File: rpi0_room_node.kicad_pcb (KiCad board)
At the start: 2 copper layers, 65 x 30 mm, 41 parts, among them J1 Raspberry Pi, J2 Conn_01x03, J3 Conn_01x03, J4 Conn_01x03, Q1 PDTC123Y, U1 AP2210K-3.3, U2 TSOP382xx, U3 RFM69HCW

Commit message: Convert to KiCad 6 format
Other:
- net class ANT removed
- net class Default removed

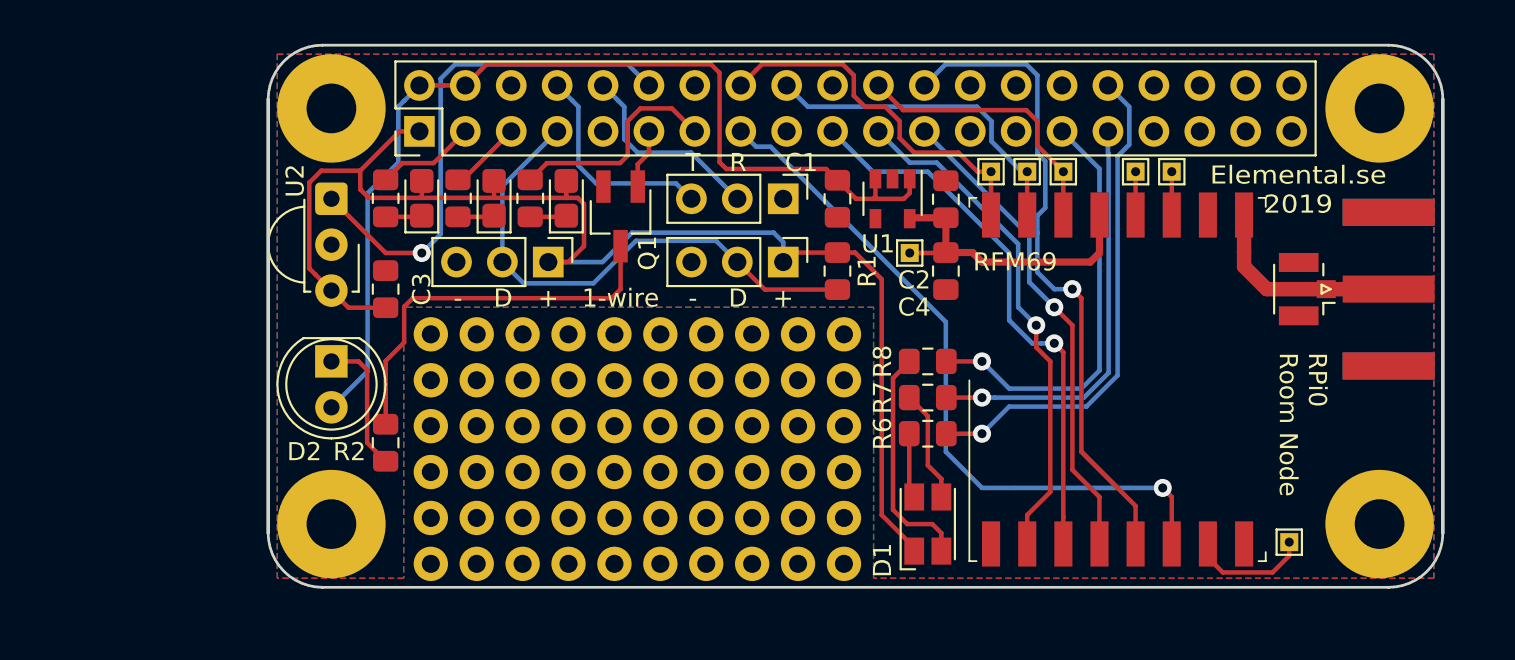
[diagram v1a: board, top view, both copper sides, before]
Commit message: Add ADS1015 ADC
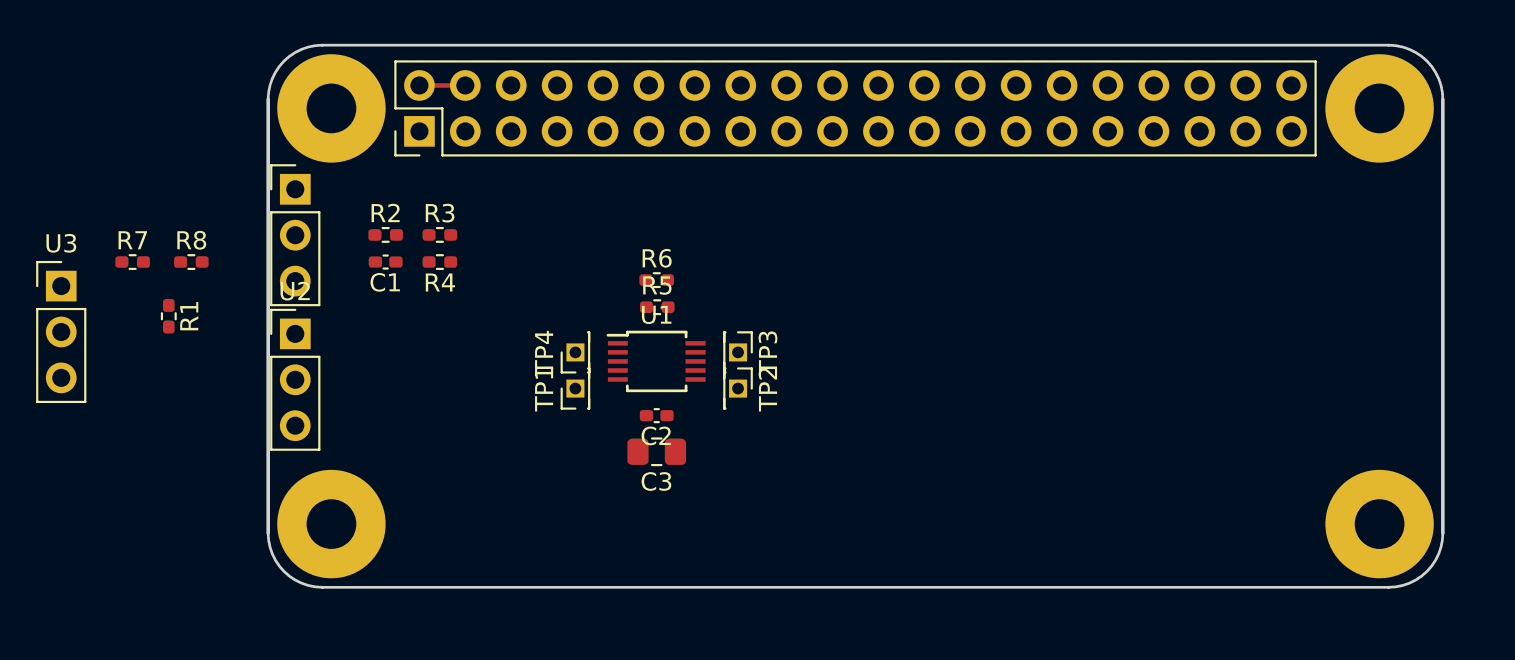
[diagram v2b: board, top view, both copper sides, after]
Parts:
- removed AE1: SMA, Connector_Coaxial:SMA_Amphenol_132289_EdgeMount
- removed AE2: U.FL, Connector_Coaxial:U.FL_Hirose_U.FL-R-SMT-1_Vertical
- removed C4: C, Capacitor_SMD:C_0805_2012Metric_Pad1.15x1.40mm_HandSolder
- removed D1: ASMB-MTB0-0A3A2, LED_SMD:LED_Avago_PLCC4_3.2x2.8mm_CW
- removed D2: CQY99, LED_THT:LED_D5.0mm_IRGrey
- removed D3, D4, D5: LED, LED_SMD:LED_0805_2012Metric_Castellated
- removed G***: LOGO, elemental:elemental-4mm-mask
- removed G***: LOGO, elemental:elemental-25.4mm
- removed J2, J4: Conn_01x03, Connector_PinHeader_2.54mm:PinHeader_1x03_P2.54mm_Vertical
- removed Q1: PDTC123Y, Package_TO_SOT_SMD:SC-59_Handsoldering
- removed REF**: protoarea, protoarea:protoarea
- removed TP5, TP6, TP7: TestPoint, TestPoint:TestPoint_THTPad_1.0x1.0mm_Drill0.5mm
- C1, C2: value C -> 100n; footprint Capacitor_SMD:C_0805_2012Metric_Pad1.15x1.40mm_HandSolder -> Capacitor_SMD:C_0402_1005Metric_Pad0.74x0.62mm_HandSolder
- C3: footprint Capacitor_SMD:C_0805_2012Metric_Pad1.15x1.40mm_HandSolder -> Capacitor_SMD:C_0805_2012Metric_Pad1.18x1.45mm_HandSolder
- R1, R2, R3, R4, R5, R6: footprint Resistor_SMD:R_0805_2012Metric_Pad1.15x1.40mm_HandSolder -> Resistor_SMD:R_0402_1005Metric_Pad0.72x0.64mm_HandSolder
- R7, R8: value R -> 10; footprint Resistor_SMD:R_0805_2012Metric_Pad1.15x1.40mm_HandSolder -> Resistor_SMD:R_0402_1005Metric_Pad0.72x0.64mm_HandSolder
- TP1, TP2, TP3, TP4: footprint TestPoint:TestPoint_THTPad_1.0x1.0mm_Drill0.5mm -> Connector_PinHeader_1.27mm:PinHeader_1x01_P1.27mm_Vertical
- U1: value AP2210K-3.3 -> ADS1015IDGS; footprint Package_TO_SOT_SMD:SOT-23-5 -> Package_SO:TSSOP-10_3x3mm_P0.5mm
- U2: value TSOP382xx -> DS18B20; footprint OptoDevice:Vishay_MINICAST-3Pin -> Connector_PinHeader_2.54mm:PinHeader_1x03_P2.54mm_Vertical
- U3: value RFM69HCW -> DS18B20; footprint RF_Module:HOPERF_RFM69HW -> Connector_PinHeader_2.54mm:PinHeader_1x03_P2.54mm_Vertical
- moved U3 58.7 mm to (85.0, 109.8), turned to 0 degrees
- moved R7 44.6 mm to (89.0, 108.5), turned to 0 degrees
- moved R8 41.1 mm to (92.2, 108.5), turned to 0 degrees
- moved TP1 40.4 mm to (113.5, 115.5), turned to 90 degrees
- moved R1 37.1 mm to (91.0, 111.5)
- moved J3 27.0 mm to (98.0, 104.5), turned to 0 degrees
- moved TP3 26.0 mm to (122.5, 113.5), turned to -90 degrees
- moved C1 25.2 mm to (103.0, 108.5), turned to 180 degrees
- moved TP4 25.1 mm to (113.5, 113.5), turned to 90 degrees
- moved TP2 25.1 mm to (122.5, 115.5), turned to -90 degrees
- moved C2 20.0 mm to (118.0, 117.0), turned to 180 degrees
- moved C3 17.5 mm to (118.0, 119.0), turned to 180 degrees
- moved R6 17.2 mm to (118.0, 109.5), turned to 0 degrees
- moved U1 15.9 mm to (118.0, 114.0), turned to 0 degrees
- moved R2 11.5 mm to (103.0, 107.0), turned to 0 degrees
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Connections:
- C1 pad 1: +5V -> /AIN0
- C2 pad 1: VDDA -> +3.3V
- C3 pad 1: +3V3 -> +3.3V
- J1 pad 1: +3V3 -> +3.3V
- J1 pad 10: /RXD -> unconnected-(J1-Pad10)
- J1 pad 11: /IRTX -> unconnected-(J1-Pad11)
- J1 pad 12: /IRRX -> unconnected-(J1-Pad12)
- J1 pad 13: /LED3 -> unconnected-(J1-Pad13)
- J1 pad 14: GND -> unconnected-(J1-Pad14)
- J1 pad 15: /RFM_RST -> unconnected-(J1-Pad15)
- J1 pad 16: /RFM_DIO2 -> unconnected-(J1-Pad16)
- J1 pad 17: Net-(J1-Pad17) -> unconnected-(J1-Pad17)
- J1 pad 18: /RFM_DIO1 -> unconnected-(J1-Pad18)
- J1 pad 19: /MOSI -> unconnected-(J1-Pad19)
- J1 pad 20: GND -> unconnected-(J1-Pad20)
- J1 pad 21: /MISO -> unconnected-(J1-Pad21)
- J1 pad 22: /RFM_DIO0 -> unconnected-(J1-Pad22)
- J1 pad 23: /SCLK -> unconnected-(J1-Pad23)
- J1 pad 24: /CE0 -> unconnected-(J1-Pad24)
- J1 pad 25: GND -> unconnected-(J1-Pad25)
- J1 pad 26: Net-(J1-Pad26) -> unconnected-(J1-Pad26)
- J1 pad 27: Net-(J1-Pad27) -> unconnected-(J1-Pad27)
- J1 pad 28: Net-(J1-Pad28) -> unconnected-(J1-Pad28)
- J1 pad 29: /LEDR -> unconnected-(J1-Pad29)
- J1 pad 3: /LED1 -> /SDA
- J1 pad 30: GND -> unconnected-(J1-Pad30)
- J1 pad 31: /LEDG -> unconnected-(J1-Pad31)
- J1 pad 32: /LEDB -> unconnected-(J1-Pad32)
- J1 pad 33: Net-(J1-Pad33) -> unconnected-(J1-Pad33)
- J1 pad 34: GND -> unconnected-(J1-Pad34)
- J1 pad 35: Net-(J1-Pad35) -> unconnected-(J1-Pad35)
- J1 pad 36: Net-(J1-Pad36) -> unconnected-(J1-Pad36)
- J1 pad 37: Net-(J1-Pad37) -> unconnected-(J1-Pad37)
- J1 pad 38: Net-(J1-Pad38) -> unconnected-(J1-Pad38)
- J1 pad 39: GND -> unconnected-(J1-Pad39)
- J1 pad 40: Net-(J1-Pad40) -> unconnected-(J1-Pad40)
- J1 pad 5: /LED2 -> /SCL
- J1 pad 7: /ONEWIRE -> Net-(J1-Pad7)
- J1 pad 8: /TXD -> unconnected-(J1-Pad8)
- J1 pad 9: GND -> unconnected-(J1-Pad9)
- J3 pad 2: /RXD -> /AI0
- J3 pad 3: /TXD -> +3.3V
- R1 pad 1: +3V3 -> +3.3V
- R2 pad 1: Net-(D2-Pad1) -> /AI0
- R2 pad 2: Net-(Q1-Pad3) -> /AIN0
- R3 pad 1: /LED1 -> /AIN0
- R3 pad 2: Net-(D3-Pad1) -> +3.3V
- R4 pad 1: /LED2 -> GND
- R4 pad 2: Net-(D4-Pad1) -> /AIN0
- R5 pad 1: /LED3 -> Net-(R5-Pad1)
- R5 pad 2: Net-(D5-Pad1) -> +3.3V
- R6 pad 1: /LEDB -> Net-(R5-Pad1)
- R6 pad 2: Net-(D1-Pad2) -> GND
- R7 pad 1: /LEDG -> Net-(J1-Pad7)
- R7 pad 2: Net-(D1-Pad3) -> /ONEWIRE
- R8 pad 1: /LEDR -> +3.3V
- R8 pad 2: Net-(D1-Pad4) -> /1W_VDD
- TP1 pad 1: /RFM_DIO5 -> Net-(TP1-Pad1)
- TP2 pad 1: /RFM_DIO4 -> Net-(TP2-Pad1)
- TP3 pad 1: /RFM_DIO3 -> Net-(TP3-Pad1)
- TP4 pad 1: /RFM_DIO2 -> Net-(TP4-Pad1)
- U1 pad 1: +5V -> Net-(R5-Pad1)
- U1 pad 2: GND -> Net-(TP4-Pad1)
- U1 pad 3: +5V -> GND
- U1 pad 4: Net-(U1-Pad4) -> /AIN0
- U1 pad 5: VDDA -> Net-(TP1-Pad1)
- U2 pad 1: /IRRX -> GND
- U2 pad 2: GND -> /ONEWIRE
- U2 pad 3: +3V3 -> /1W_VDD
- U3 pad 2: /MISO -> /ONEWIRE
- U3 pad 3: /MOSI -> /1W_VDD
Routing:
- net +3V3: track 75.4 -> 0.00 mm
- net +5V: track 55.5 -> 2.54 mm
- net /RFM_RST: track 39.0 -> 0.00 mm, vias 1 -> 0
- net /CE0: track 39.0 -> 0.00 mm, vias 1 -> 0
- net /MOSI: track 30.6 -> 0.00 mm, vias 1 -> 0
- net /ONEWIRE: track 29.6 -> 0.00 mm
- net /IRRX: track 28.7 -> 0.00 mm, vias 1 -> 0
- net /MISO: track 28.2 -> 0.00 mm, vias 1 -> 0
- net /LEDB: track 27.6 -> 0.00 mm, vias 1 -> 0
- net /SCLK: track 26.8 -> 0.00 mm, vias 1 -> 0
- net /LEDR: track 23.6 -> 0.00 mm, vias 1 -> 0
- net /LEDG: track 22.9 -> 0.00 mm, vias 1 -> 0
- net Net-(Q1-Pad3): track 21.7 -> 0.00 mm
- net /RFM_DIO2: track 20.4 -> 0.00 mm
- net /RFM_DIO1: track 18.3 -> 0.00 mm
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- removed copper zone on B.Cu, net GND
- removed copper zone on F.Cu, net GND
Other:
- board text removed: "+"
- board text removed: "-"
- board text removed: "0"
- board text removed: "1"
- board text removed: "1-wire"
- board text removed: "1wire"
- board text removed: "2"
- board text removed: "3"
- board text removed: "3.3V"
- board text removed: "4"
- board text removed: "5"
- board text removed: "D"
- board text removed: "Elemental.se 2019"
- board text removed: "GND"
- board text removed: "IR RX"
- board text removed: "IR TX"
- board text removed: "R"
- board text removed: "RFM 3V3"
- board text removed: "RFM DIO"
- board text removed: "RFM69"
- board text removed: "RPi0 Room Node"
- board text removed: "SMA"
- board text removed: "T"
- board text removed: "serial"

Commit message: Add one-wire chip
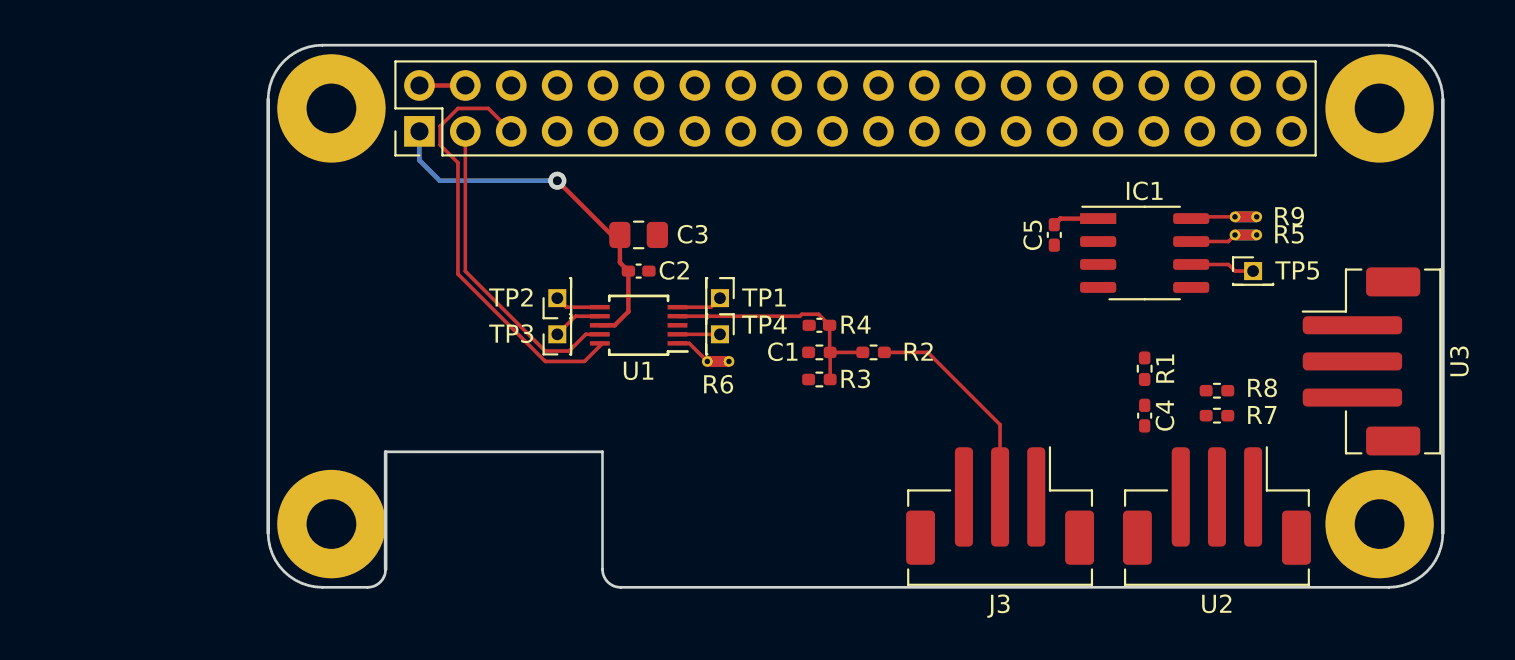
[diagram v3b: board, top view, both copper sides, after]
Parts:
- added C4: 100n, Capacitor_SMD:C_0402_1005Metric_Pad0.74x0.62mm_HandSolder, F.Cu at (145.0, 117.0)
- added C5: 100n, Capacitor_SMD:C_0402_1005Metric_Pad0.74x0.62mm_HandSolder, F.Cu at (140.0, 107.0)
- added IC1: DS2482-100S, Package_SO:SO-8_3.9x4.9mm_P1.27mm, F.Cu at (145.0, 108.0)
- added R9: R, NetTie:NetTie-2_THT_Pad0.3mm, F.Cu at (151.2, 106.0)
- added TP5: TestPoint, Connector_PinHeader_1.27mm:PinHeader_1x01_P1.27mm_Vertical, F.Cu at (151.0, 109.0)
- J3, U2, U3: footprint Connector_PinHeader_2.54mm:PinHeader_1x03_P2.54mm_Vertical -> Connector_JST:JST_PH_B3B-PH-SM4-TB_1x03-1MP_P2.00mm_Vertical
- R5, R6: footprint Resistor_SMD:R_0402_1005Metric_Pad0.72x0.64mm_HandSolder -> NetTie:NetTie-2_THT_Pad0.3mm
- moved U3 72.1 mm to (157.0, 114.0), turned to -90 degrees
- moved R7 60.6 mm to (149.0, 117.0)
- moved R8 57.2 mm to (149.0, 115.6)
- moved R1 54.1 mm to (145.0, 114.4)
- moved U2 51.9 mm to (149.0, 122.0), turned to 180 degrees
- moved J3 42.8 mm to (137.0, 122.0), turned to 180 degrees
- moved R5 33.4 mm to (151.2, 107.0), turned to 180 degrees
- moved R2 27.8 mm to (130.0, 113.5), turned to 180 degrees
- moved C1 24.3 mm to (127.0, 112.0)
- moved R3 22.5 mm to (127.0, 115.0), turned to 180 degrees
- moved R4 21.6 mm to (127.0, 113.5), turned to 0 degrees
- moved C3 12.0 mm to (117.0, 107.0), turned to 0 degrees
- moved TP2 11.2 mm to (112.5, 110.5), turned to 90 degrees
- moved TP3 10.0 mm to (112.5, 112.5), turned to 90 degrees
- moved TP1 9.43 mm to (121.5, 110.5), turned to -90 degrees
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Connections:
- R1 pad 1: +3.3V -> /1W_VDD
- R5 pad 1: Net-(R5-Pad1) -> GND
- R5 pad 2: +3.3V -> Net-(IC1-Pad7)
- R6 pad 1: Net-(R5-Pad1) -> GND
- R6 pad 2: GND -> Net-(R6-Pad2)
- U1 pad 1: Net-(R5-Pad1) -> Net-(R6-Pad2)
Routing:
- net /SCL: track 0.00 -> 24.0 mm
- net +3.3V: track 0.00 -> 23.3 mm, vias 0 -> 1
- net /SDA: track 0.00 -> 17.4 mm
- net /AIN0: track 0.00 -> 13.5 mm
- net /AI0: track 0.00 -> 12.1 mm
- net Net-(IC1-Pad6): track 0.00 -> 3.58 mm
- net Net-(TP3-Pad1): track 0.00 -> 2.76 mm
- net Net-(IC1-Pad7): track 0.00 -> 2.58 mm
- net Net-(TP2-Pad1): track 0.00 -> 2.56 mm
- net Net-(TP1-Pad1): track 0.00 -> 2.56 mm
- net Net-(IC1-Pad8): track 0.00 -> 2.46 mm
- net Net-(TP4-Pad1): track 0.00 -> 2.35 mm
- net Net-(R6-Pad2): track 0.00 -> 2.21 mm
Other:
- outline, holes or cut-outs redrawn

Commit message: Polishing
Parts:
- removed TP1: TestPoint, Connector_PinHeader_1.27mm:PinHeader_1x01_P1.27mm_Vertical
- added C6: 100n, Capacitor_SMD:C_0603_1608Metric_Pad1.08x0.95mm_HandSolder, F.Cu at (112.0, 114.0)
- added G***: LOGO, elemental:elemental-4mm-mask, F.Cu at (125.5, 123.5)
- added G***: LOGO, elemental:elemental-25.4mm, B.Cu at (128.5, 122.0)
- added J2: Conn_01x03, Connector_JST:JST_PH_B3B-PH-SM4-TB_1x03-1MP_P2.00mm_Vertical, F.Cu at (101.0, 114.0)
- added R10: R, Resistor_SMD:R_0603_1608Metric_Pad0.98x0.95mm_HandSolder, F.Cu at (108.0, 114.0)
- added R11: R, Resistor_SMD:R_0603_1608Metric_Pad0.98x0.95mm_HandSolder, F.Cu at (111.0, 112.0)
- added R12: R, Resistor_SMD:R_0603_1608Metric_Pad0.98x0.95mm_HandSolder, F.Cu at (111.0, 116.0)
- C1: footprint Capacitor_SMD:C_0402_1005Metric_Pad0.74x0.62mm_HandSolder -> Capacitor_SMD:C_0603_1608Metric_Pad1.08x0.95mm_HandSolder
- C3: value 1u -> DNP
- R2, R3, R4: footprint Resistor_SMD:R_0402_1005Metric_Pad0.72x0.64mm_HandSolder -> Resistor_SMD:R_0603_1608Metric_Pad0.98x0.95mm_HandSolder
- moved C1 11.5 mm to (138.5, 112.0), turned to 90 degrees
- moved R4 10.3 mm to (137.0, 111.0), turned to -90 degrees
- moved R3 9.01 mm to (135.5, 112.0), turned to 90 degrees
- moved TP4 8.50 mm to (130.0, 112.5)
- moved C2 7.50 mm to (124.5, 109.0)
- moved C3 7.50 mm to (124.5, 107.0)
- moved R6 7.50 mm to (129.5, 114.0)
- moved TP2 7.50 mm to (120.0, 110.5)
- moved TP3 7.50 mm to (120.0, 112.5)
- moved U1 7.50 mm to (124.5, 112.0)
- moved R2 7.16 mm to (137.0, 115.0), turned to 90 degrees
- moved C4 6.02 mm to (149.0, 112.5), turned to 0 degrees
- moved R1 4.77 mm to (149.0, 117.0), turned to 0 degrees
- moved R8 1.62 mm to (149.0, 114.0)
- moved R7 1.50 mm to (149.0, 115.5)
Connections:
- J1 pad 14: unconnected-(J1-Pad14) -> GND
- J1 pad 20: unconnected-(J1-Pad20) -> GND
- J1 pad 25: unconnected-(J1-Pad25) -> GND
- J1 pad 30: unconnected-(J1-Pad30) -> GND
- J1 pad 34: unconnected-(J1-Pad34) -> GND
- J1 pad 39: unconnected-(J1-Pad39) -> GND
- J1 pad 9: unconnected-(J1-Pad9) -> GND
- U1 pad 5: Net-(TP1-Pad1) -> /AIN1
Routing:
- net +3.3V: track 23.3 -> 115.4 mm, vias 1 -> 5
- net /SDA: track 17.4 -> 70.2 mm
- net /SCL: track 24.0 -> 69.5 mm, vias 0 -> 1
- net Net-(J1-Pad7): track 0.00 -> 44.5 mm, vias 0 -> 1
- net /AIN1: track 0.00 -> 28.6 mm
- net GND: track 0.00 -> 28.3 mm, vias 0 -> 9
- net /ONEWIRE: track 0.00 -> 26.6 mm
- net /1W_VDD: track 0.00 -> 25.2 mm, vias 0 -> 3
- net /AI0: track 12.1 -> 5.90 mm
- net /AI1: track 0.00 -> 5.90 mm
- net Net-(TP1-Pad1): track 2.56 -> 0.00 mm
- net Net-(TP4-Pad1): track 2.35 -> 3.76 mm
- net /AIN0: track 13.5 -> 14.9 mm
- added copper zone on B.Cu, net GND
- added copper zone on F.Cu, net GND
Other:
- board text added: "1W"
- board text added: "AIN0"
- board text added: "AIN1"
- board text added: "RPi0 ADC/1W hat Jonas Norling 2023"

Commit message: Clean up, round corners
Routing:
- net +3.3V: track 115.4 -> 108.9 mm
- net GND: track 28.3 -> 27.2 mm
- net /SDA: track 70.2 -> 69.3 mm
- net Net-(J1-Pad7): track 44.5 -> 43.8 mm
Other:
- outline, holes or cut-outs redrawn
